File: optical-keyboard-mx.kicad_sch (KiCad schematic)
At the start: 6 parts, among them U1 BlackPill_STLINK

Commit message: Python scripts to add curved tracks
Script to place mouting holes, draw edge cuts.

A  MyFootprints.pretty/SMTSO_M1.6.kicad_mod
A  MyFootprints.pretty/SMTSO_M2.kicad_mod
A  drawborder.py
M  optical-keyboard-mx.kicad_pcb
M  optical-keyboard-mx.kicad_prl
M  optical-keyboard-mx.kicad_sch
A  placeholes.py
M  placemx.py
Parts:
- added H1, H10, H11, H12, H13, H14, H15, H16, H17, H2, H3, H4, H5, H6, H7, H8, H9: MountingHole, MyFootprints:SMTSO_M2, symbol Mechanical:MountingHole

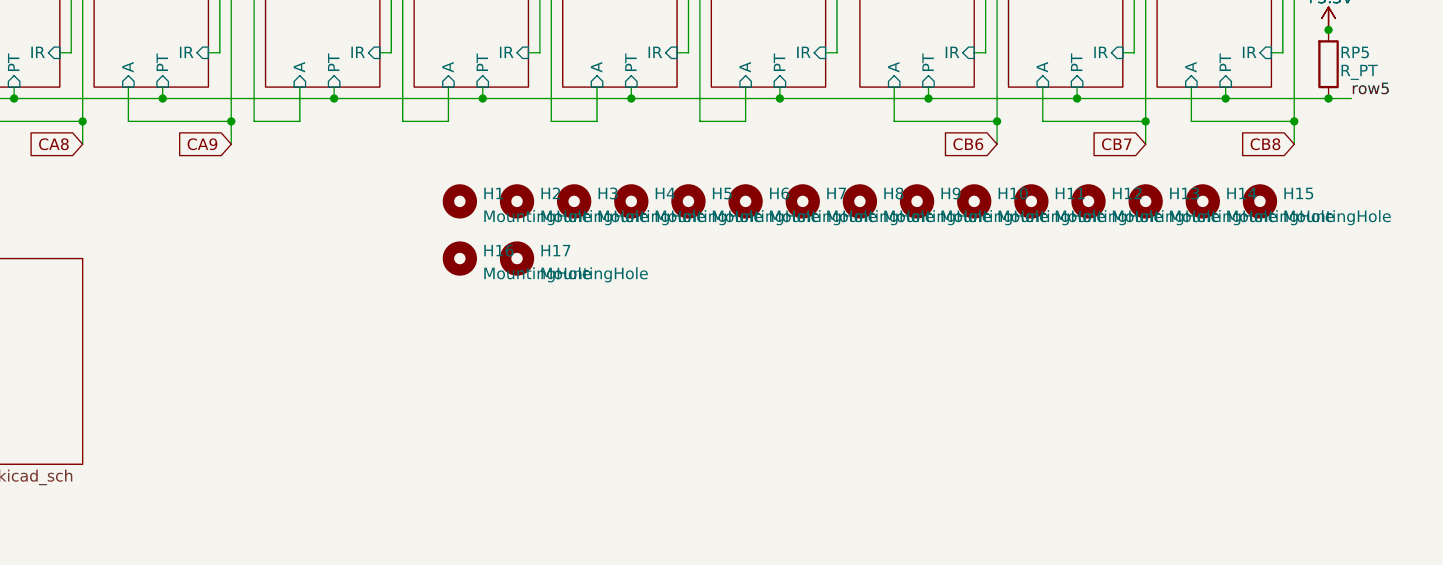
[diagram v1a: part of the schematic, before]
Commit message: Add python script to draw edge cuts
M  MyFootprints.pretty/BlackPill_STLINK_Down.kicad_mod
A  MyFootprints.pretty/MountingHole_1.7mm_M1.6_Pad.kicad_mod
A  MyFootprints.pretty/MountingHole_2.2mm_M2_ISO7380_Pad.kicad_mod
A  MyFootprints.pretty/PinHeader_1x04_P2.54mm_Vertical.kicad_mod
A  MyFootprints.pretty/PinHeader_1x08_P2.54mm_Vertical.kicad_mod
M  MySymbols.kicad_sym
M  drawborder.py
A  mounting-hw.kicad_sch
M  optical-keyboard-mx.kicad_pcb
M  optical-keyboard-mx.kicad_prl
M  optical-keyboard-mx.kicad_pro
M  optical-keyboard-mx.kicad_sch
M  placeholes.py
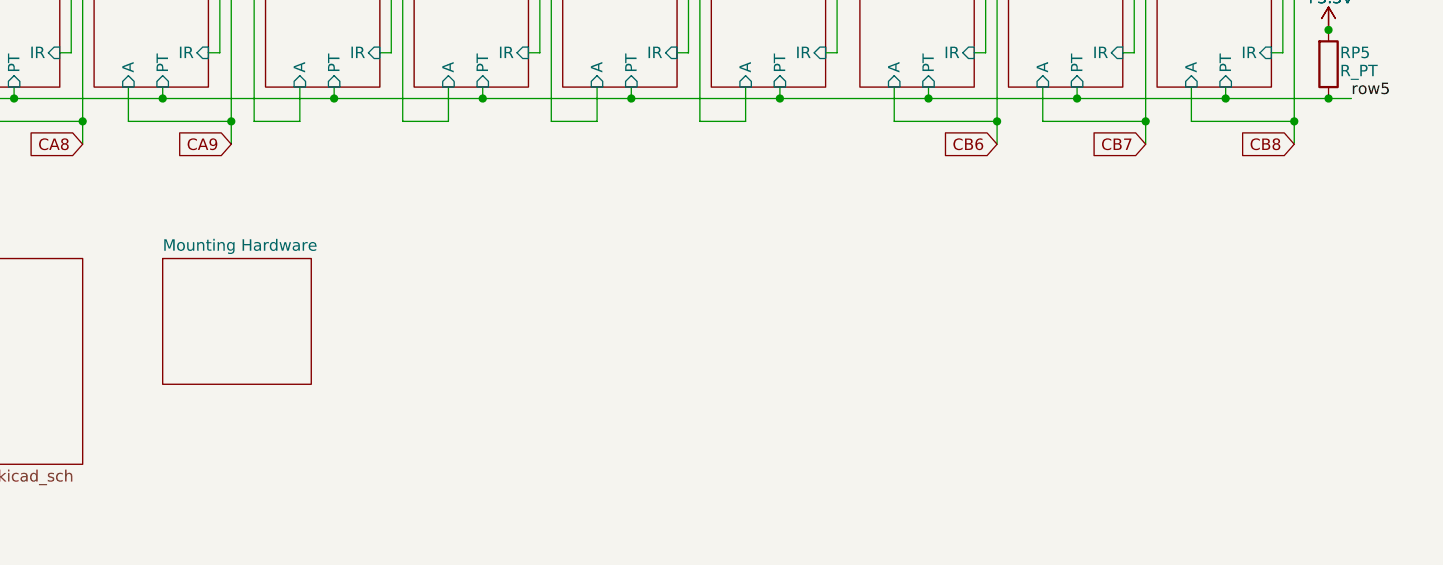
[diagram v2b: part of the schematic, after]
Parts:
- removed H1, H10, H11, H12, H13, H14, H15, H16, H17, H2, H3, H4, H5, H6, H7, H8, H9: MountingHole, MyFootprints:SMTSO_M2, symbol Mechanical:MountingHole
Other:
- added sheet Mounting Hardware (mounting-hw.kicad_sch)

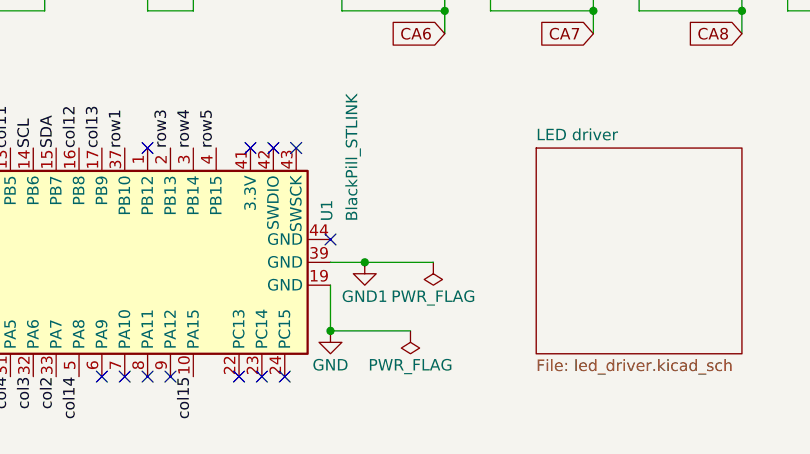
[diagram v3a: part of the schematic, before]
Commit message: Tracks laid, wrist support and switch plate
M  MyFootprints.pretty/BlackPill_STLINK_Down.kicad_mod
M  MyFootprints.pretty/SMTSO_M1.6.kicad_mod
M  MyFootprints.pretty/SMTSO_M2.kicad_mod
M  MyFootprints.pretty/Switch_Cutout.kicad_mod
D  MyFootprints.pretty/Switch_Cutout_1.25u.kicad_mod
D  MyFootprints.pretty/Switch_Cutout_1.5u.kicad_mod
D  MyFootprints.pretty/Switch_Cutout_1.75u.kicad_mod
M  MySymbols.kicad_sym
M  drawborder.py
M  led_driver.kicad_sch
M  mounting-hw.kicad_sch
M  optical-keyboard-mx.kicad_pcb
M  optical-keyboard-mx.kicad_prl
M  optical-keyboard-mx.kicad_pro
M  optical-keyboard-mx.kicad_sch
M  placefp.py
 D placefpg.mx
M  placeholes.py
A  switch-plate/.gitignore
A  switch-plate/fp-lib-table
A  switch-plate/switch-plate.kicad_pcb
A  switch-plate/switch-plate.kicad_prl
A  switch-plate/switch-plate.kicad_pro
A  switch-plate/switch-plate.kicad_sch
A  switch-plate/sym-lib-table
M  switch.kicad_sch
A  wrist-support/.gitignore
A  wrist-support/fp-lib-table
A  wrist-support/sym-lib-table
A  wrist-support/wrist-support.kicad_pcb
A  wrist-support/wrist-support.kicad_prl
A  wrist-support/wrist-support.kicad_pro
A  wrist-support/wrist-support.kicad_sch
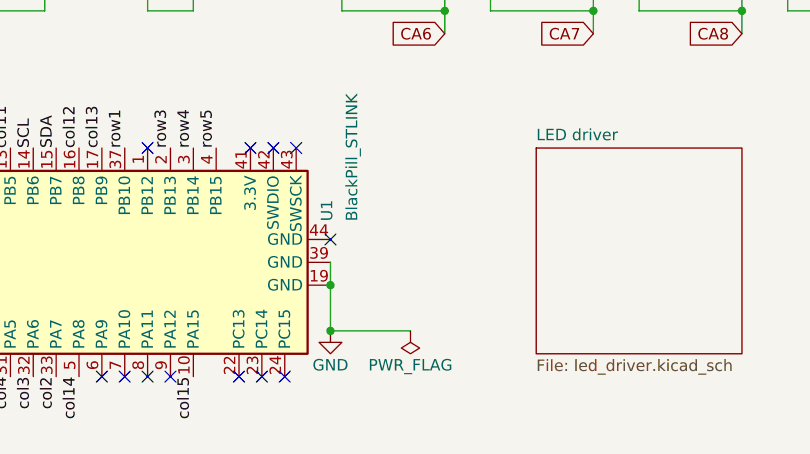
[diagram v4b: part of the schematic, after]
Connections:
- net GND1 is gone; now on net GND: U1.39 (GND)

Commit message: Add gerbers and assembly files
M  .gitignore
M  MyFootprints.pretty/MountingHole_2.2mm_M2_ISO7380_Pad.kicad_mod
M  MySymbols.kicad_sym
M  README.md
M  drawborder.py
A  jlcpcb/gerber/optical-keyboard-mx-B_Cu.gbl
A  jlcpcb/gerber/optical-keyboard-mx-B_Mask.gbs
A  jlcpcb/gerber/optical-keyboard-mx-B_Paste.gbp
A  jlcpcb/gerber/optical-keyboard-mx-B_Silkscreen.gbo
A  jlcpcb/gerber/optical-keyboard-mx-Edge_Cuts.gm1
A  jlcpcb/gerber/optical-keyboard-mx-F_Cu.gtl
A  jlcpcb/gerber/optical-keyboard-mx-F_Mask.gts
A  jlcpcb/gerber/optical-keyboard-mx-F_Paste.gtp
A  jlcpcb/gerber/optical-keyboard-mx-F_Silkscreen.gto
A  jlcpcb/gerber/optical-keyboard-mx-NPTH-drl_map.gbr
A  jlcpcb/gerber/optical-keyboard-mx-NPTH.drl
A  jlcpcb/gerber/optical-keyboard-mx-PTH-drl_map.gbr
A  jlcpcb/gerber/optical-keyboard-mx-PTH.drl
M  led_driver.kicad_sch
M  mounting-hw.kicad_sch
M  optical-keyboard-mx.kicad_pcb
M  optical-keyboard-mx.kicad_sch
M  placefp.py
M  switch-plate/.gitignore
A  switch-plate/jlcpcb/gerber/switch-plate-B_Cu.gbl
A  switch-plate/jlcpcb/gerber/switch-plate-B_Mask.gbs
A  switch-plate/jlcpcb/gerber/switch-plate-B_Paste.gbp
A  switch-plate/jlcpcb/gerber/switch-plate-B_Silkscreen.gbo
A  switch-plate/jlcpcb/gerber/switch-plate-Edge_Cuts.gm1
A  switch-plate/jlcpcb/gerber/switch-plate-F_Cu.gtl
A  switch-plate/jlcpcb/gerber/switch-plate-F_Mask.gts
A  switch-plate/jlcpcb/gerber/switch-plate-F_Paste.gtp
A  switch-plate/jlcpcb/gerber/switch-plate-F_Silkscreen.gto
A  switch-plate/jlcpcb/gerber/switch-plate-NPTH-drl_map.gbr
A  switch-plate/jlcpcb/gerber/switch-plate-NPTH.drl
A  switch-plate/jlcpcb/gerber/switch-plate-PTH-drl_map.gbr
A  switch-plate/jlcpcb/gerber/switch-plate-PTH.drl
M  switch-plate/switch-plate.kicad_pcb
M  switch-plate/switch-plate.kicad_prl
M  switch.kicad_sch
M  wrist-support/.gitignore
A  wrist-support/jlcpcb/gerber/wrist-support-B_Cu.gbl
A  wrist-support/jlcpcb/gerber/wrist-support-B_Mask.gbs
A  wrist-support/jlcpcb/gerber/wrist-support-B_Paste.gbp
A  wrist-support/jlcpc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
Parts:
- RP1, RP2, RP3, RP4, RP5: LCSC C17713 -> C17633
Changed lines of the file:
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@@
       (effects (font (size 0.5 0.5)) hide)
     )
-    (property "LCSC" "C17713" (id 5) (at 280.67 41.91 0)
-      (effects (font (size 0.5 0.5)) hide)
-    )
-    (pin "1")
-    (pin "2")
-  )
-  (symbol (lib_id "MySymbols:R_PT") (at 276.86 69.85 0) (unit 1)
+    (property "LCSC" "C17633" (id 5) (at 280.67 41.91 0)
+      (effects (font (size 0.5 0.5)) hide)
+    )
+    (pin "1")
+    (pin "2")
+  )
+  (symbol (lib_name "R_PT_4") (lib_id "MySymbols:R_PT") (at 276.86 69.85 0) (unit 1)
     (in_bom yes) (on_board yes) (fields_autoplaced)
     (property "Reference" "RP2" (id 0) (at 278.13 68.58 0)
@@
       (effects (font (size 0.5 0.5)) hide)
     )
-    (property "LCSC" "C17713" (id 5) (at 280.67 66.04 0)
+    (property "LCSC" "C17633" (id 5) (at 280.67 66.04 0)
       (effects (font (size 0.5 0.5)) hide)
     )
@@
     (pin "1")
   )
-  (symbol (lib_id "MySymbols:R_PT") (at 276.86 93.98 0) (unit 1)
+  (symbol (lib_name "R_PT_3") (lib_id "MySymbols:R_PT") (at 276.86 93.98 0) (unit 1)
     (in_bom yes) (on_board yes) (fields_autoplaced)
     (property "Reference" "RP3" (id 0) (at 278.13 92.71 0)
@@
       (effects (font (size 0.5 0.5)) hide)
     )
-    (property "LCSC" "C17713" (id 5) (at 280.67 90.17 0)
+    (property "LCSC" "C17633" (id 5) (at 280.67 90.17 0)
       (effects (font (size 0.5 0.5)) hide)
     )
@@
     (pin "9")
   )
-  (symbol (lib_id "MySymbols:R_PT") (at 276.86 118.11 0) (unit 1)
+  (symbol (lib_name "R_PT_1") (lib_id "MySymbols:R_PT") (at 276.86 118.11 0) (unit 1)
     (in_bom yes) (on_board yes) (fields_autoplaced)
     (property "Reference" "RP4" (id 0) (at 278.13 116.84 0)
@@
       (effects (font (size 0.5 0.5)) hide)
     )
-    (property "LCSC" "C17713" (id 5) (at 280.67 114.3 0)
+    (property "LCSC" "C17633" (id 5) (at 280.67 114.3 0)
       (effects (font (size 0.5 0.5)) hide)
     )
@@
     (pin "1")
   )
-  (symbol (lib_id "MySymbols:R_PT") (at 276.86 142.24 0) (unit 1)
+  (symbol (lib_name "R_PT_2") (lib_id "MySymbols:R_PT") (at 276.86 142.24 0) (unit 1)
     (in_bom yes) (on_board yes) (fields_autoplaced)
     (property "Reference" "RP5" (id 0) (at 278.13 140.97 0)
@@
       (effects (font (size 0.5 0.5)) hide)
     )
-    (property "LCSC" "C17713" (id 5) (at 280.67 138.43 0)
-      (effects (font (size 0.5 0.5)) hide)
-    )
+    (property "LCSC" "C17633" (id 5) (at 280.67 138.43 0)
+      (effects (font (size 0.5 0.5)) hide)
+    )

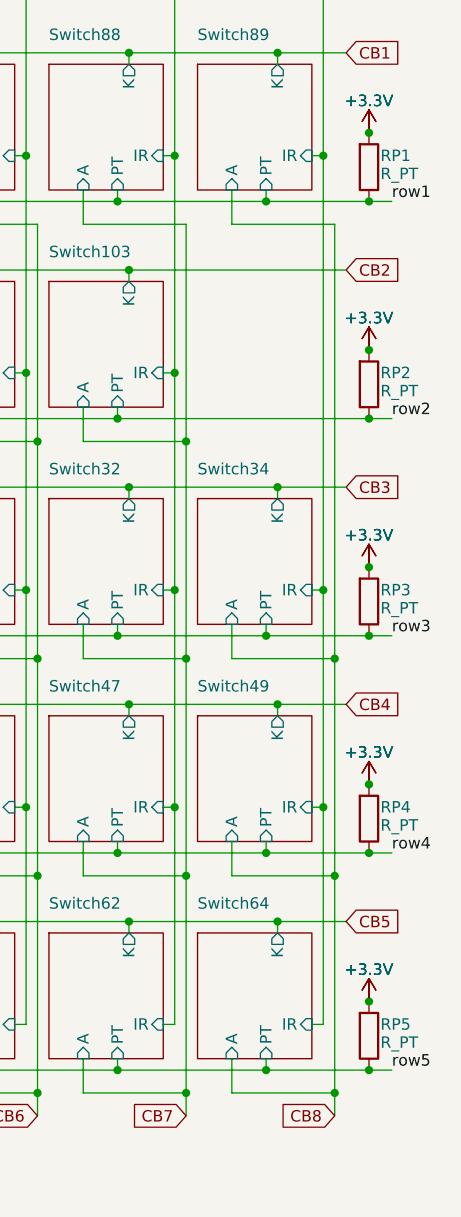
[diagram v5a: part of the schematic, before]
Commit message: updated part numbers for jlcpcb
M  MySymbols.kicad_sym
M  drawborder.py
M  optical-keyboard-mx.kicad_sch
M  switch.kicad_sch
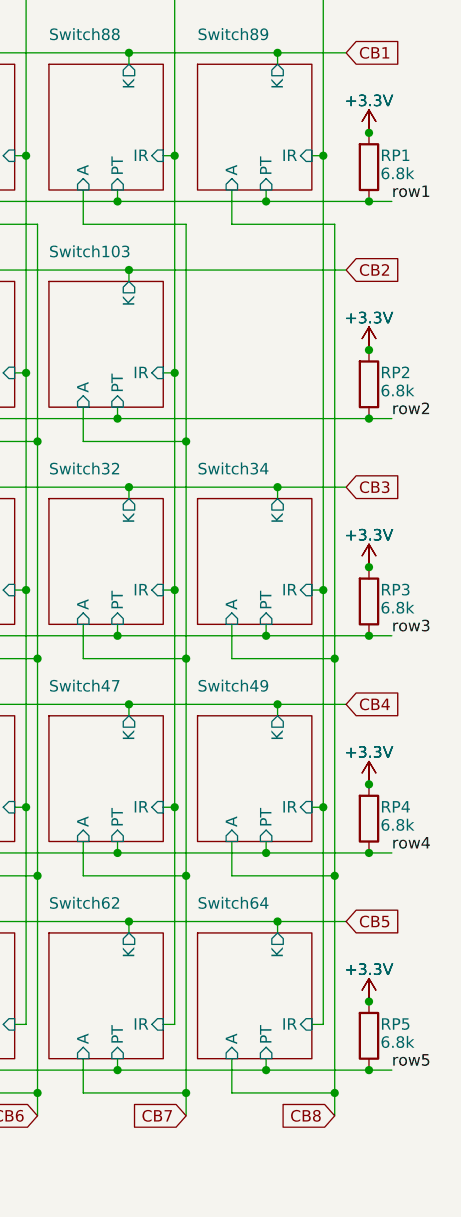
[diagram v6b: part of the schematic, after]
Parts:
- RP1, RP2, RP3, RP4, RP5: value R_PT -> 6.8k; LCSC C17633 -> C269547
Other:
- company: (none) -> girish
- title: (none) -> Optical Keyboard Gateron MX

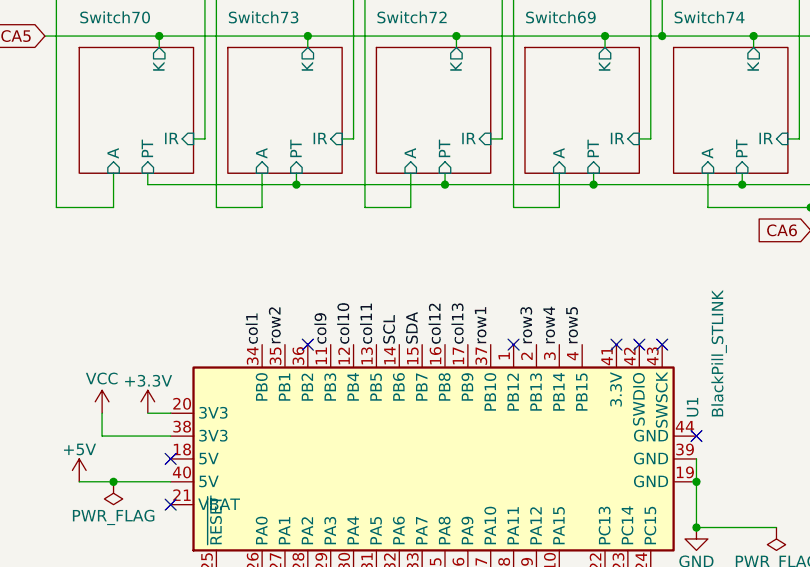
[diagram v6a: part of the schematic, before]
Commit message: Fix bug where SCL SDA of I2c not connected
M  drawborder.py
M  led_driver.kicad_sch
M  optical-keyboard-mx.kicad_pcb
M  optical-keyboard-mx.kicad_prl
M  optical-keyboard-mx.kicad_sch
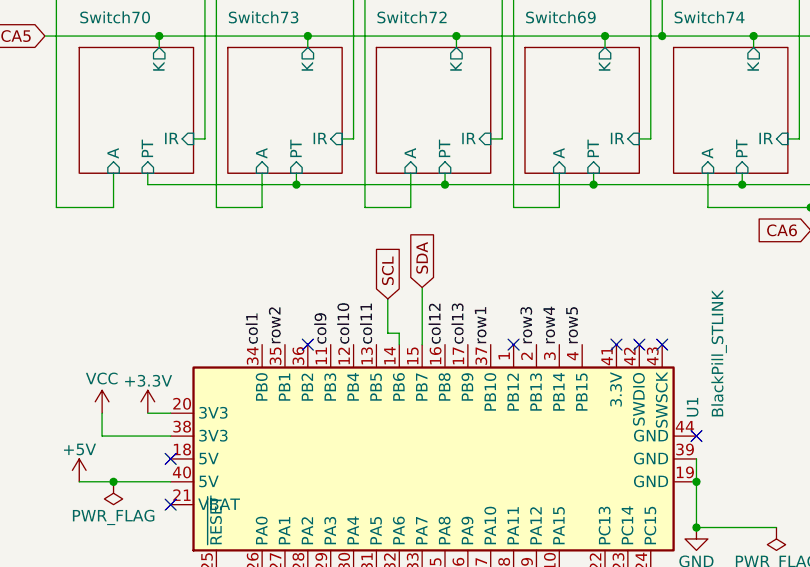
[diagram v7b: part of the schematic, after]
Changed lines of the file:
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@@
+    (stroke (width 0) (type default) (color 0 0 0 0))
+  )
+  (wire (pts (xy 58.42 158.75) (xy 58.42 162.56))
     (stroke (width 0) (type default) (color 0 0 0 0))
   )
@@
     (stroke (width 0) (type default) (color 0 0 0 0))
   )
+  (wire (pts (xy 59.69 163.83) (xy 59.69 162.56))
+    (stroke (width 0) (type default) (color 0 0 0 0))
+  )
   (wire (pts (xy 172.72 44.45) (xy 172.72 68.58))
     (stroke (width 0) (type default) (color 0 0 0 0))
@@
     (stroke (width 0) (type default) (color 0 0 0 0))
   )
+  (wire (pts (xy 62.23 157.48) (xy 62.23 163.83))
+    (stroke (width 0) (type default) (color 0 0 0 0))
+  )
   (wire (pts (xy 130.81 120.65) (xy 130.81 121.92))
     (stroke (width 0) (type default) (color 0 0 0 0))
@@
     (stroke (width 0) (type default) (color 0 0 0 0))
   )
+  (wire (pts (xy 59.69 162.56) (xy 58.42 162.56))
+    (stroke (width 0) (type default) (color 0 0 0 0))
+  )
   (wire (pts (xy 143.51 76.2) (xy 154.94 76.2))
     (stroke (width 0) (type default) (color 0 0 0 0))
@@
   )
   (label "col1" (at 44.45 163.83 90)
-    (effects (font (size 1.27 1.27)) (justify left bottom))
-  )
-  (label "SCL" (at 59.69 163.83 90)
     (effects (font (size 1.27 1.27)) (justify left bottom))
   )
@@
     (effects (font (size 1.27 1.27)) (justify left bottom))
   )
-  (label "SDA" (at 62.23 163.83 90)
-    (effects (font (size 1.27 1.27)) (justify left bottom))
-  )
   (label "col5" (at 54.61 189.23 270)
     (effects (font (size 1.27 1.27)) (justify right bottom))
@@
   (label "row1" (at 279.4 49.53 0)
     (effects (font (size 1.27 1.27)) (justify left bottom))
+  )
+  (global_label "SDA" (shape input) (at 62.23 157.48 90) (fields_autoplaced)
+    (effects (font (size 1.27 1.27)) (justify left))
+    (property "Intersheet References" "${INTERSHEET_REFS}" (id 0) (at 62.1506 151.4988 90)
+      (effects (font (size 1.27 1.27)) (justify left) hide)
+    )
   )
   (global_label "CB6" (shape input) (at 240.03 151.13 180) (fields_autoplaced)
@@
       (effects (font (size 1.27 1.27)) (justify left) hide)
     )
+  )
+  (global_label "SCL" (shape input) (at 58.42 158.75 90) (fields_autoplaced)
+    (effects (font (size 1.27 1.27)) (justify left))
+    (property "Intersheet References" "${INTERSHEET_REFS}" (id 0) (at 58.3406 152.8293 90)
+      (effects (font (size 1.27 1.27)) (justify left) hide)
+    )
